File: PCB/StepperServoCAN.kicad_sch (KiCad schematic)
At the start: 132 parts, among them J1 CAR, J2 Debug, J3 Motor, J4 Conn_01x06, Q1 AO3401A, Q2 2N7002, Q3 AO3401A, SW1 Rst, SW2 Fcn>, SW3 Fcn>, U2 STM32F103CBT6, U3 LMV321, U4 AT8236, U5 DRV8870, U6 LMV321, U7 TLE5012B, U8 TMAG5170-Q1, U9 SN65HVD230, Y1 16Mhz 9pF

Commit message: Nema23 holes follow StepperOnline dimensions
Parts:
- H1, H2, H3, H4: footprint MountingHole:MountingHole_2.7mm_M2.5_ISO14580_Pad_TopOnly -> MountingHole:MountingHole_3.2mm_M3_ISO14580_Pad_TopOnly
- R34: footprint Resistor_SMD:R_0805_2012Metric -> Resistor_SMD:R_0402_1005Metric_Pad0.72x0.64mm_HandSolder; LCSC C17673 -> C2906941
- R35: footprint Resistor_SMD:R_0805_2012Metric -> Resistor_SMD:R_0402_1005Metric_Pad0.72x0.64mm_HandSolder
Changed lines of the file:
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@@
 			)
 		)
-		(property "Footprint" "Resistor_SMD:R_0805_2012Metric"
+		(property "Footprint" "Resistor_SMD:R_0402_1005Metric_Pad0.72x0.64mm_HandSolder"
 			(at 203.2 135.636 0)
 			(effects
@@
 			)
 		)
-		(property "LCSC" "C17673"
+		(property "LCSC" "C2906941"
 			(at 200.66 135.636 0)
 			(effects
@@
 			)
 		)
-		(property "Footprint" "Resistor_SMD:R_0805_2012Metric"
+		(property "Footprint" "Resistor_SMD:R_0402_1005Metric_Pad0.72x0.64mm_HandSolder"
 			(at 217.424 135.636 0)
 			(effects
@@
 			)
 		)
-		(property "Footprint" "MountingHole:MountingHole_2.7mm_M2.5_ISO14580_Pad_TopOnly"
+		(property "Footprint" "MountingHole:MountingHole_3.2mm_M3_ISO14580_Pad_TopOnly"
 			(at 156.972 154.178 0)
 			(effects
@@
 			)
 		)
-		(property "Footprint" "MountingHole:MountingHole_2.7mm_M2.5_ISO14580_Pad_TopOnly"
+		(property "Footprint" "MountingHole:MountingHole_3.2mm_M3_ISO14580_Pad_TopOnly"
 			(at 172.212 154.178 0)
 			(effects
@@
 			)
 		)
-		(property "Footprint" "MountingHole:MountingHole_2.7mm_M2.5_ISO14580_Pad_TopOnly"
+		(property "Footprint" "MountingHole:MountingHole_3.2mm_M3_ISO14580_Pad_TopOnly"
 			(at 172.212 164.338 0)
 			(effects
@@
 			)
 		)
-		(property "Footprint" "MountingHole:MountingHole_2.7mm_M2.5_ISO14580_Pad_TopOnly"
+		(property "Footprint" "MountingHole:MountingHole_3.2mm_M3_ISO14580_Pad_TopOnly"
 			(at 156.972 164.338 0)
 			(effects

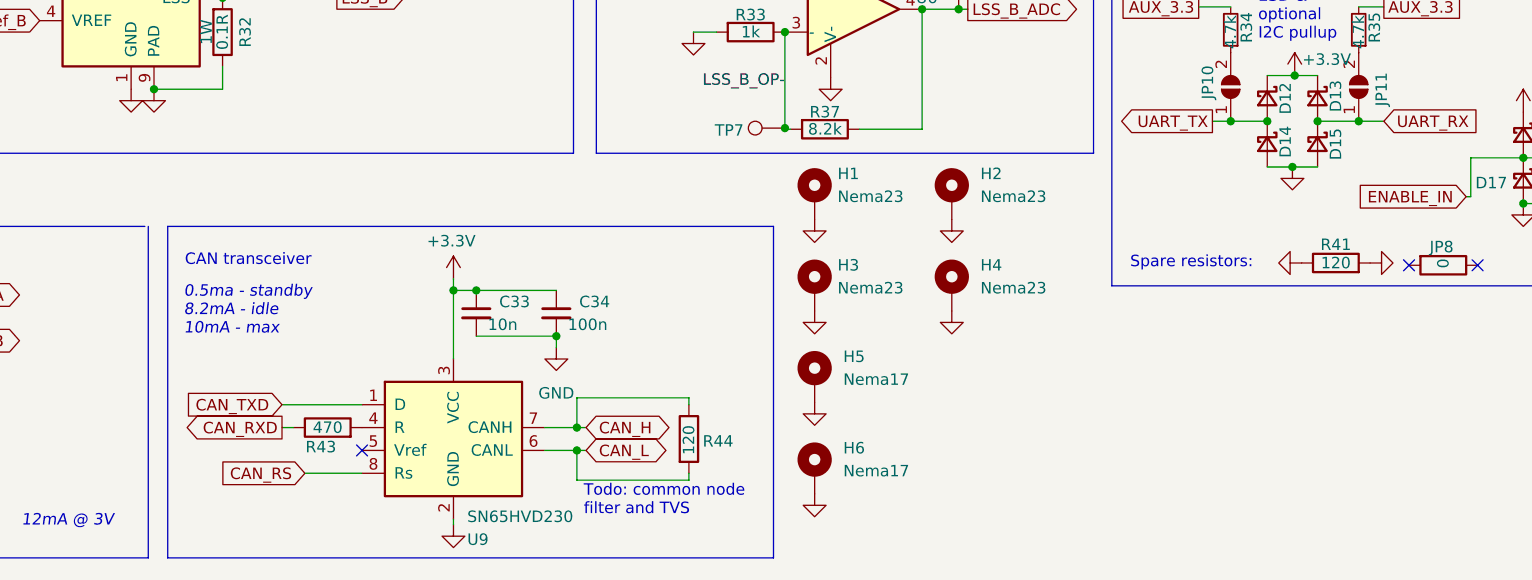
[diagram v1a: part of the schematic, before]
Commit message: relocated termination resistor for easy access
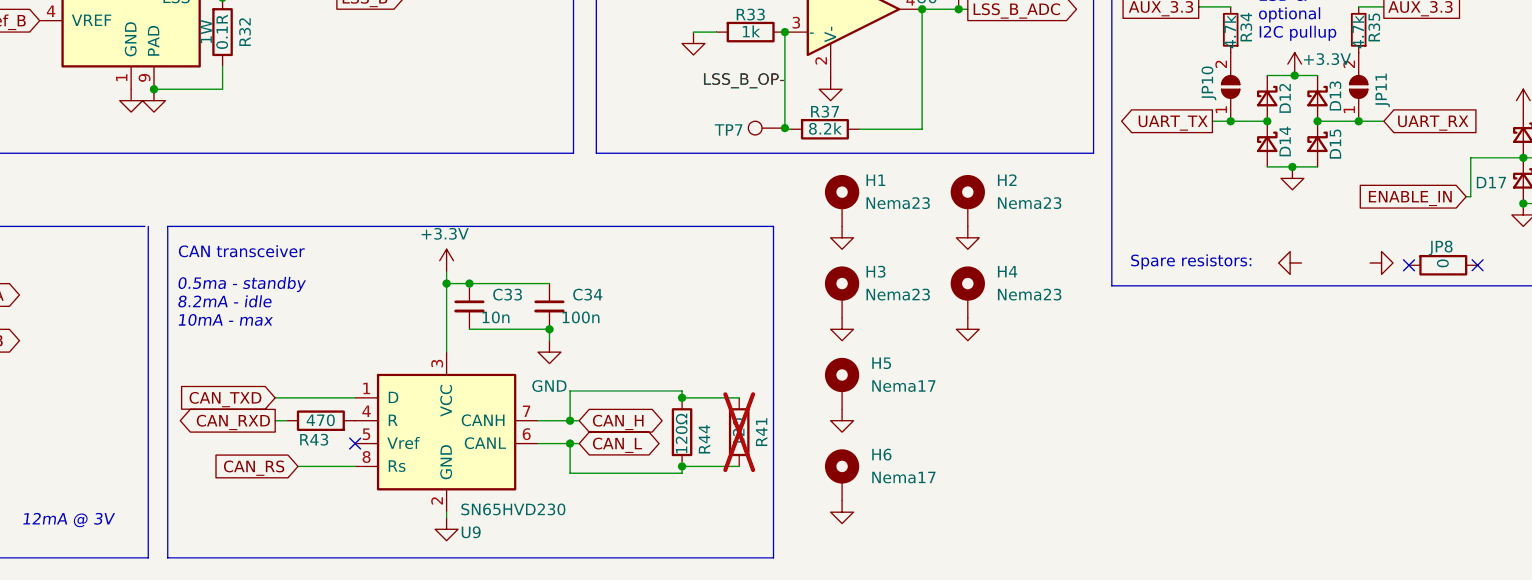
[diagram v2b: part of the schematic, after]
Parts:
- R34: footprint Resistor_SMD:R_0402_1005Metric_Pad0.72x0.64mm_HandSolder -> Resistor_SMD:R_0805_2012Metric_Pad1.20x1.40mm_HandSolder; LCSC C2906941 -> C17673
- R35: footprint Resistor_SMD:R_0402_1005Metric_Pad0.72x0.64mm_HandSolder -> Resistor_SMD:R_0805_2012Metric_Pad1.20x1.40mm_HandSolder
- R41: now not fitted
- R44: value 120 -> 120Ω
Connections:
- net CAN_H: now also R41.2
- net CAN_L: now also R41.1
- net GND: no longer R41.1, R41.2
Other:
- note removed: "Todo: common node filter and TVS"
- moved on the sheet: C33, C34, H1, H2, H3, H4, H5, H6, R43, R44, U9

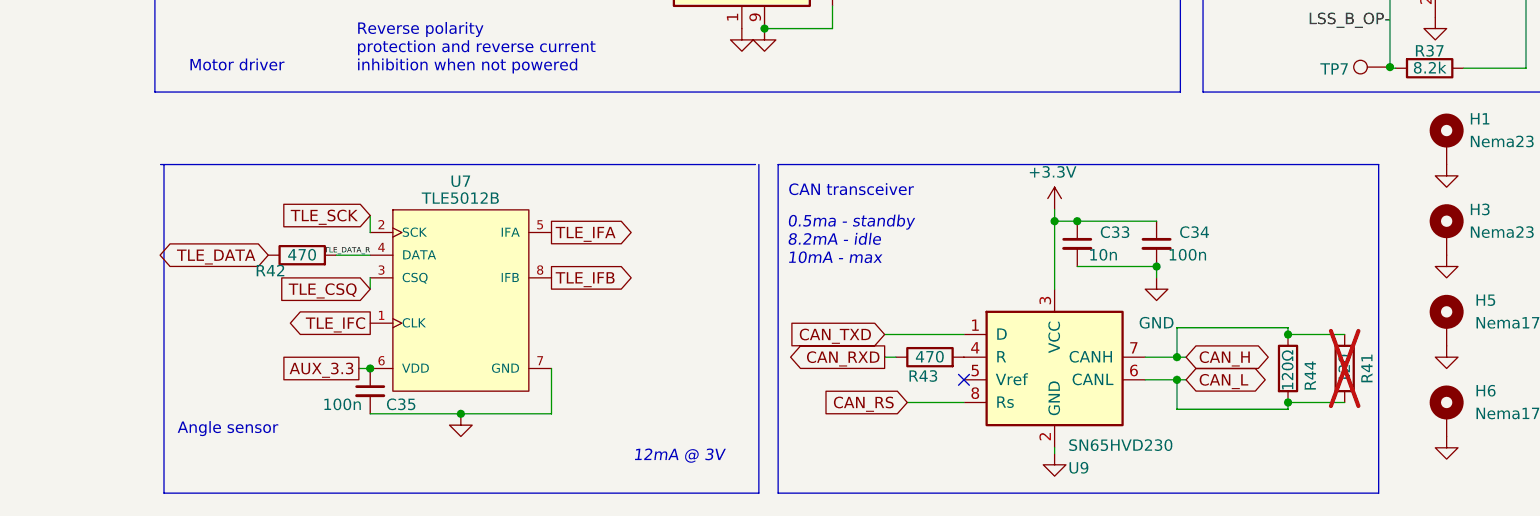
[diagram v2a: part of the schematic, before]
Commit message: PESD1CAN esd protection
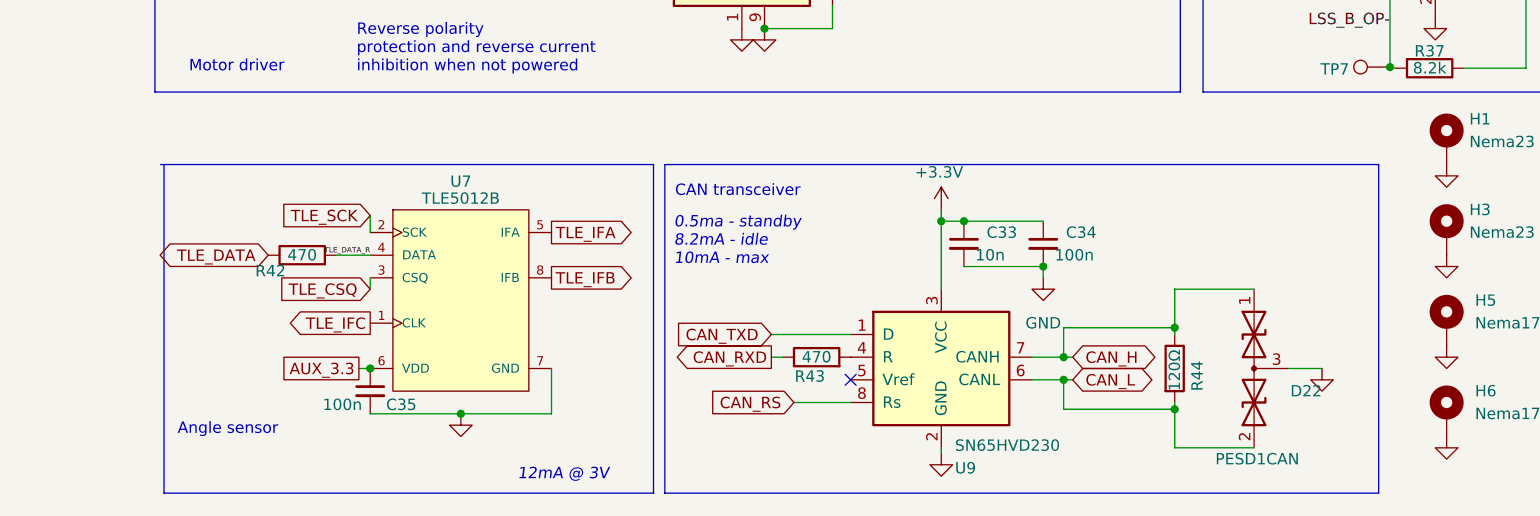
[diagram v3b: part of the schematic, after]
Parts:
- removed R41: 120, Resistor_SMD:R_1206_3216Metric_Pad1.30x1.75mm_HandSolder, symbol Device:R
- added D22: PESD1CAN, Package_TO_SOT_SMD:SOT-23, symbol Device:D_TVS_Dual_AAC
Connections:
- net CAN_H: now also D22.1 (A1)
- net CAN_L: now also D22.2 (A2)
- net GND: now also D22.3 (common)
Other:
- moved on the sheet: C33, C34, R43, R44, U9

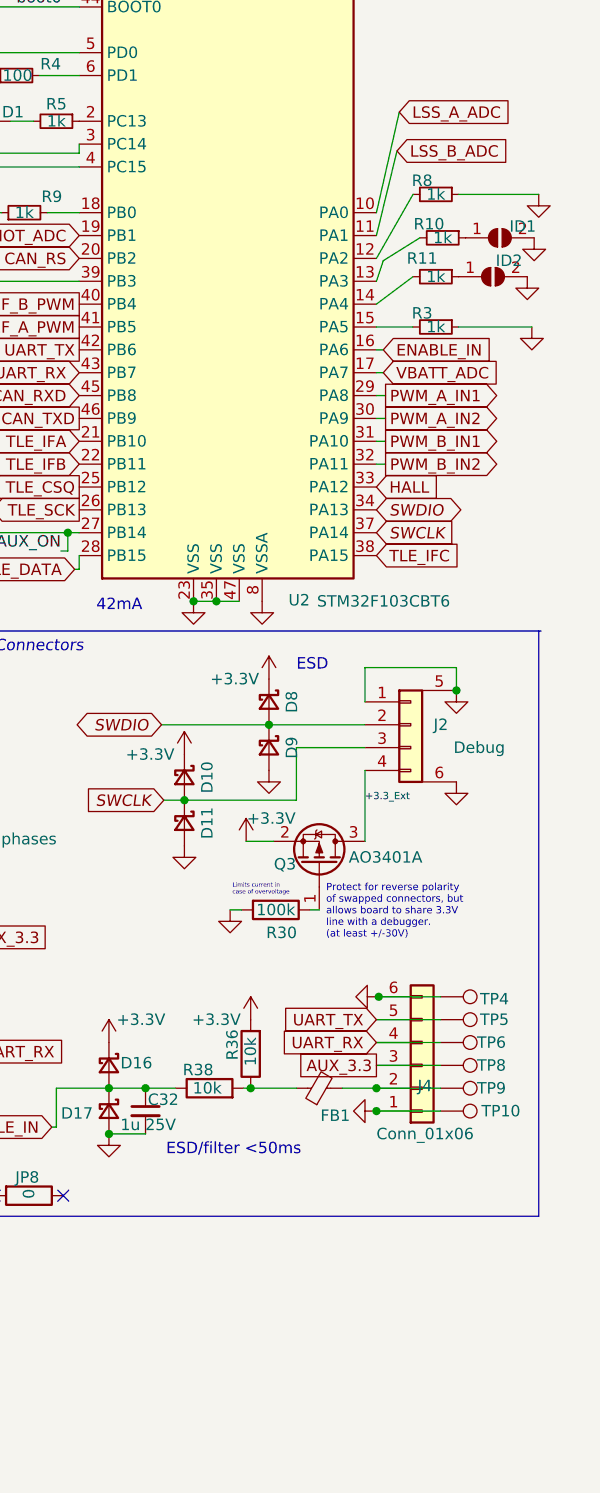
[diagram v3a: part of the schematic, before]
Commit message: Added hardware id table. Added hardware id v0.4. Currently not used.  Might be used to to set thermal/current limits depending on the hardware
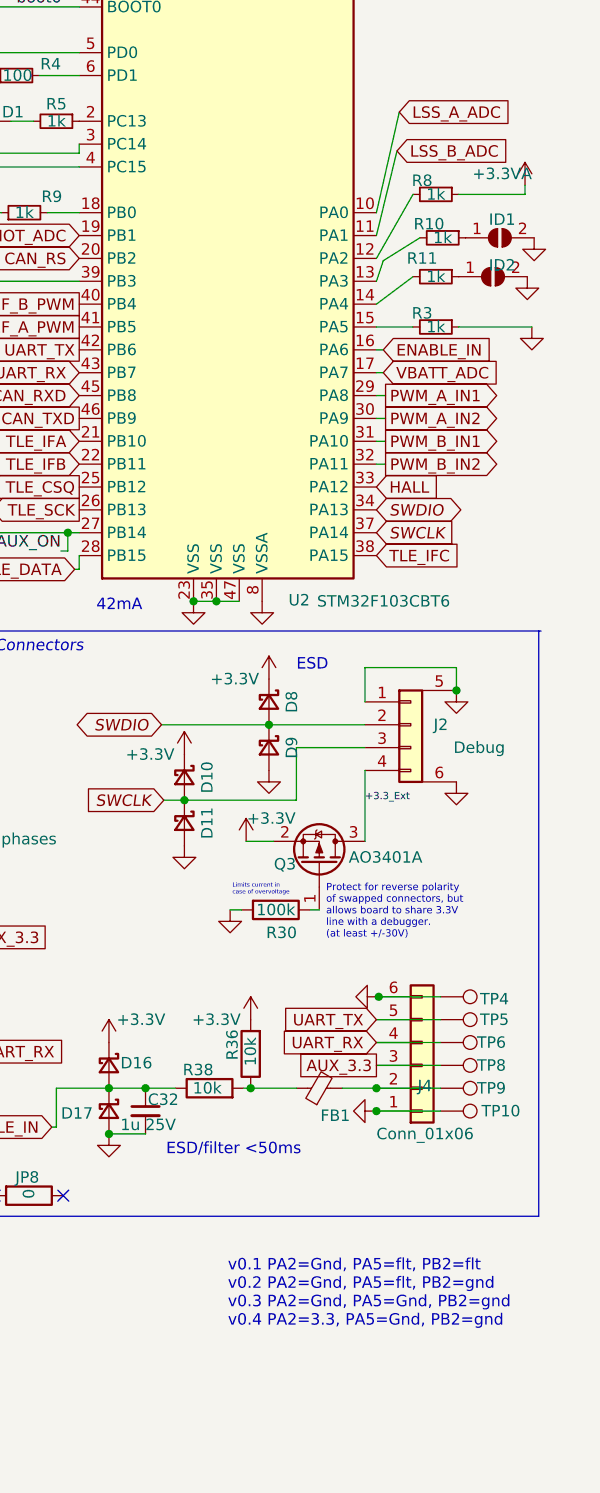
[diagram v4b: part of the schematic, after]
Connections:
- net +3.3VA: now also R8.1
- net GND: no longer R8.1
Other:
- note added: "v0.1 PA2=Gnd, PA5=flt, PB2=flt v0.2 PA2=Gnd, PA5=flt, PB2=gnd v0.3 PA2=Gnd, PA5=Gnd, PB2=gnd v0.4 PA2=3.3, PA5=Gnd, PB2=gnd"
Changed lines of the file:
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@@
 	(title_block
 		(title "StepperServoCAN")
-		(rev "0.3")
+		(rev "0.4")
 		(company "RetroPilot")
 		(comment 1 "Licensed under CERN-OHL-S v2")
@@
 	(wire
 		(pts
-			(xy 274.574 50.546) (xy 283.464 50.546)
-		)
-		(stroke
-			(width 0)
-			(type default)
-		)
-	)
-	(wire
-		(pts
 			(xy 47.752 82.296) (xy 47.752 81.788)
 		)
@@
 	(wire
 		(pts
+			(xy 281.94 50.546) (xy 274.574 50.546)
+		)
+		(stroke
+			(width 0)
+			(type default)
+		)
+	)
+	(wire
+		(pts
 			(xy 231.14 88.138) (xy 232.41 88.138)
 		)
@@
 	(wire
 		(pts
+			(xy 281.94 50.546) (xy 281.94 49.53)
+		)
+		(stroke
+			(width 0)
+			(type default)
+		)
+	)
+	(wire
+		(pts
 			(xy 105.918 168.91) (xy 114.808 168.91)
 		)
@@
 		)
 	)
+	(text "v0.1 PA2=Gnd, PA5=flt, PB2=flt\nv0.2 PA2=Gnd, PA5=flt, PB2=gnd\nv0.3 PA2=Gnd, PA5=Gnd, PB2=gnd\nv0.4 PA2=3.3, PA5=Gnd, PB2=gnd"
+		(exclude_from_sim no)
+		(at 248.92 172.72 0)
+		(effects
+			(font
+				(face "Liberation Mono")
+				(size 1.27 1.27)
+			)
+			(justify left)
+		)
+	)
 	(text "CAN transceiver\n"
 		(exclude_from_sim no)
@@
 	(symbol
 		(lib_id "power:+3.3VA")
+		(at 281.94 49.53 0)
+		(unit 1)
+		(exclude_from_sim no)
+		(in_bom yes)
+		(on_board yes)
+		(dnp no)
+		(property "Reference" "#PWR012"
+			(at 281.94 53.34 0)
+			(effects
+				(font
+					(size 1.27 1.27)
+				)
+				(hide yes)
+			)
+		)
+		(property "Value" "+3.3VA"
+			(at 279.4 48.26 0)
+			(effects
+				(font
+					(size 1.27 1.27)
+				)
+			)
+		)
+		(property "Footprint" ""
+			(at 281.94 49.53 0)
+			(effects
+				(font
+					(size 1.27 1.27)
+				)
+				(hide yes)
+			)
+		)
+		(property "Datasheet" ""
+			(at 281.94 49.53 0)
+			(effects
+				(font
+					(size 1.27 1.27)
+				)
+				(hide yes)
+			)
+		)
+		(property "Description" ""
+			(at 281.94 49.53 0)
+			(effects
+				(font
+					(size 1.27 1.27)
+				)
+				(hide yes)
+			)
+		)
+		(pin "1"
+		)
+		(instances
+			(project "StepperServoCAN"
+				(path "/92dad13e-412a-43d4-9260-9087579302b1"
+					(reference "#PWR012")
+					(unit 1)
+				)
+			)
+		)
+	)
+	(symbol
+		(lib_id "power:+3.3VA")
 		(at 158.75 90.932 0)
 		(unit 1)
@@
 	)
 	(symbol
-		(lib_id "power:GND")
-		(at 283.464 50.546 0)
-		(unit 1)
-		(exclude_from_sim no)
-		(in_bom yes)
-		(on_board yes)
-		(dnp no)
-		(property "Reference" "#PWR018"
-			(at 283.464 56.896 0)
-			(effects
-				(font
-					(size 1.27 1.27)
-				)
-				(hide yes)
-			)
-		)
-		(property "Value" "GND"
-			(at 280.924 51.816 90)
-			(effects
-				(font
-					(size 1.27 1.27)
-				)
-				(justify left)
-				(hide yes)
-			)
-		)
-		(property "Footprint" ""
-			(at 283.464 50.546 0)
-			(effects
-				(font
-					(size 1.27 1.27)
-				)
-				(hide yes)
-			)
-		)
-		(property "Datasheet" ""
-			(at 283.464 50.546 0)
-			(effects
-				(font
-					(size 1.27 1.27)
-				)
-				(hide yes)
-			)
-		)
-		(property "Description" ""
-			(at 283.464 50.546 0)
-			(effects
-				(font
-					(size 1.27 1.27)
-				)
-				(hide yes)
-			)
-		)
-		(pin "1"
-		)
-		(instances
-			(project "StepperServoCAN"
-				(path "/92dad13e-412a-43d4-9260-9087579302b1"
-					(reference "#PWR018")
-					(unit 1)
-				)
-			)
-		)
-	)
-	(symbol
 		(lib_id "Device:R")
 		(at 246.888 149.86 90)
@@
 		(dnp no)
 		(property "Reference" "ID2"
-			(at 280.162 57.912 0)
+			(at 279.4 58.42 0)
 			(effects
 				(font
@@
 		(dnp no)
 		(property "Reference" "ID1"
-			(at 281.686 54.102 0)
+			(at 279.4 53.34 0)
 			(effects
 				(font
